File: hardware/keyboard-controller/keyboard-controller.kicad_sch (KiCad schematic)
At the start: 30 parts, among them J1 Keybed_Connector, J2 Debug_Pins, J3 Barrel_Jack_Switch, J4 CV_OUT, J5 GATE_OUT, U1 L78L09_TO92, U2 LM358, U3 74HC164, U4 74HC164, U5 LM1117-3.3, U6 Pico, U7 TL431LP, U8 MCP4921

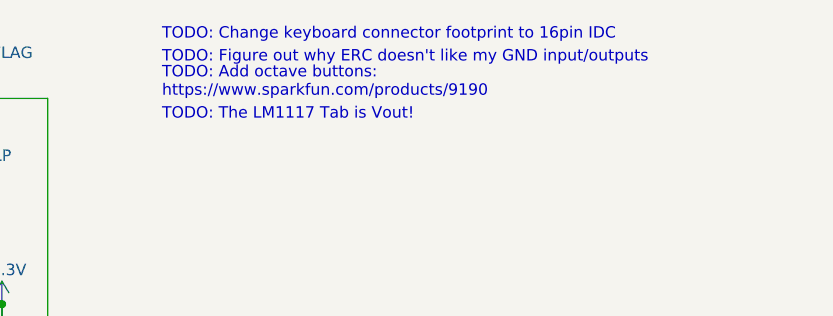
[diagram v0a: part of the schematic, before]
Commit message: Code cleanup. Switched keyboard connector to 16pin IDC
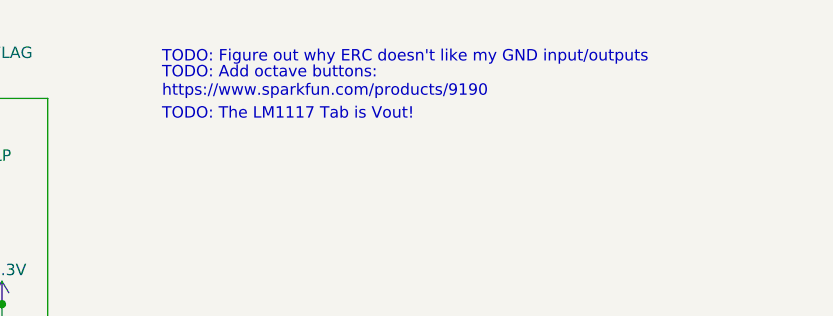
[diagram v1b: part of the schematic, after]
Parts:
- J1: footprint Connector_PinHeader_2.54mm:PinHeader_1x15_P2.54mm_Vertical -> Connector_IDC:IDC-Header_2x08_P2.54mm_Vertical
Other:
- note removed: "TODO: Change keyboard connector footprint to 16pin IDC"
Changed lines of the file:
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@@
     (stroke (width 0) (type default) (color 0 0 0 0))
-  )
-  (text "TODO: Change keyboard connector footprint to 16pin IDC"
-    (at 214.63 15.24 0)
-    (effects (font (size 1.27 1.27)) (justify left bottom))
   )
   (text "TODO: The LM1117 Tab is Vout!" (at 214.63 24.13 0)
@@
     (property "Reference" "J1" (id 0) (at 24.13 59.69 0))
     (property "Value" "Keybed_Connector" (id 1) (at 24.13 57.15 0))
-    (property "Footprint" "Connector_PinHeader_2.54mm:PinHeader_1x15_P2.54mm_Vertical" (id 2) (at 21.59 36.83 0)
+    (property "Footprint" "Connector_IDC:IDC-Header_2x08_P2.54mm_Vertical" (id 2) (at 21.59 36.83 0)
       (effects (font (size 1.27 1.27)) hide)
     )
@@
   (symbol (lib_id "power:+3.3V") (at 128.27 92.71 90) (mirror x) (unit 1)
     (in_bom yes) (on_board yes)
-    (property "Reference" "#PWR?" (id 0) (at 132.08 92.71 0)
+    (property "Reference" "#PWR0102" (id 0) (at 132.08 92.71 0)
       (effects (font (size 1.27 1.27)) hide)
     )
@@
     )
     (path "/31770e7f-32b1-45bb-a492-7d715b566d2b"
-      (reference "#PWR?") (unit 1) (value "+3.3V") (footprint "")
+      (reference "#PWR0102") (unit 1) (value "+3.3V") (footprint "")
     )
     (path "/166f34cf-82f0-4a5a-ad24-51c9547c2601"
@@
     )
     (path "/0ad4f42e-3f7d-4f1a-a0d8-8aff92bbf5d3"
-      (reference "J1") (unit 1) (value "Keybed_Connector") (footprint "Connector_PinHeader_2.54mm:PinHeader_1x15_P2.54mm_Vertical")
+      (reference "J1") (unit 1) (value "Keybed_Connector") (footprint "Connector_IDC:IDC-Header_2x08_P2.54mm_Vertical")
     )
     (path "/cf784822-648c-46a3-a790-edcd7292ca65"

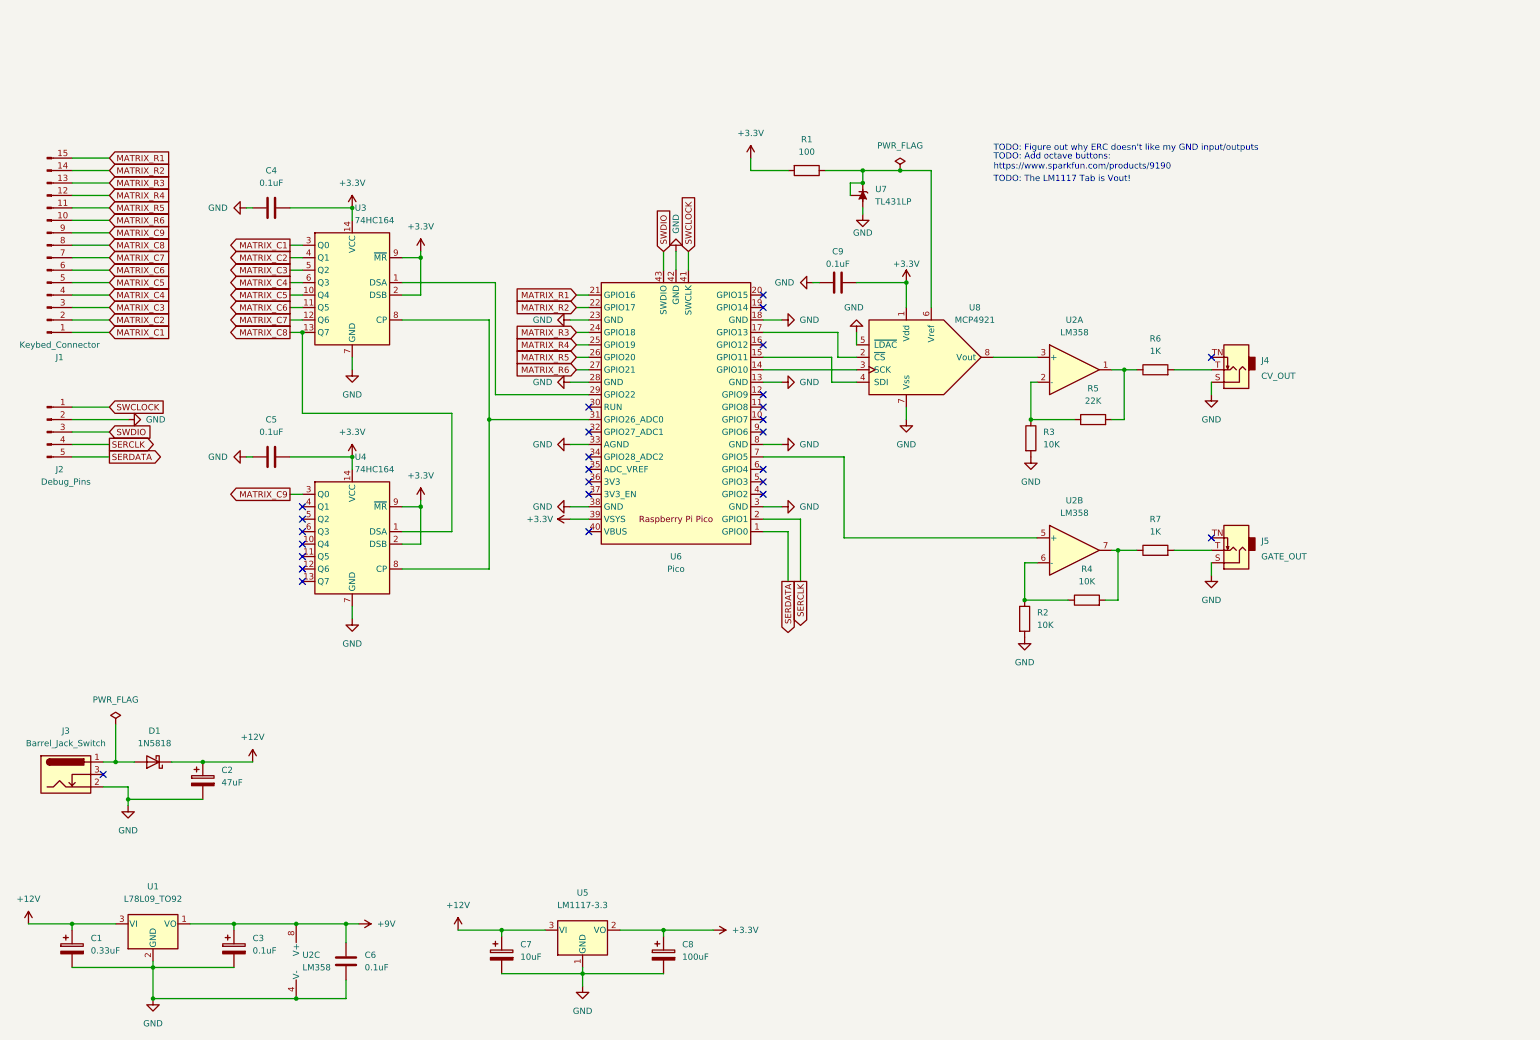
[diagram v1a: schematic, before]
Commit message: Added octave shift buttons
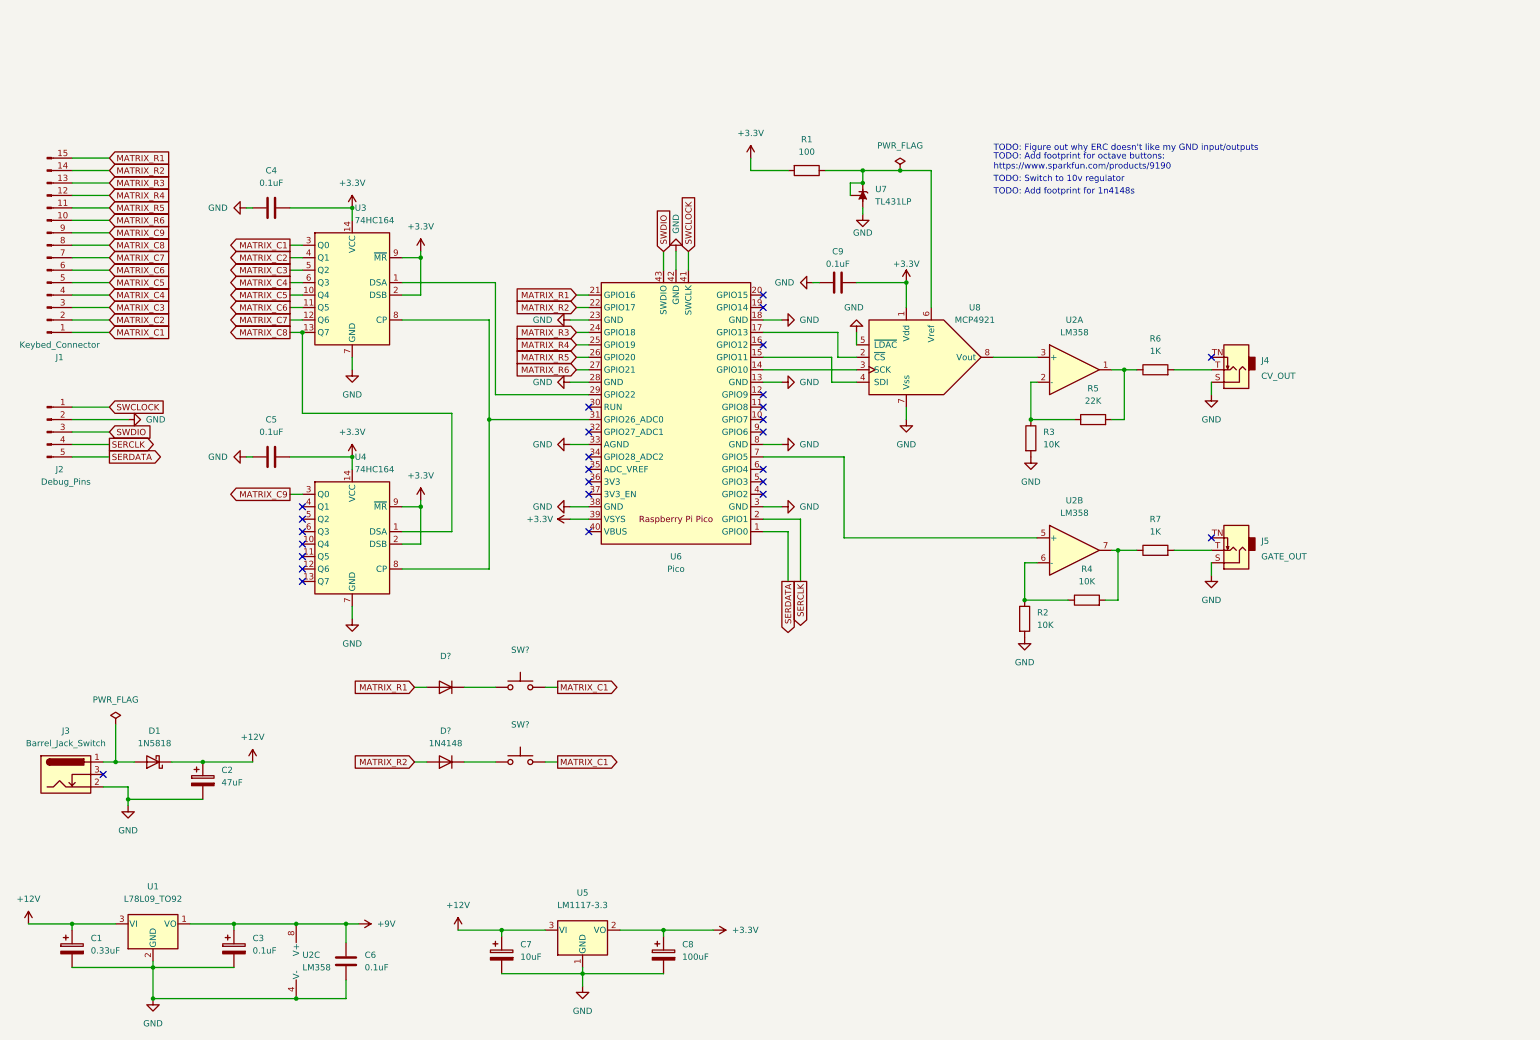
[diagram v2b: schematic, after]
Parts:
- added D?: (no value), symbol Diode:1N4148
- added D?: 1N4148, Diode_THT:D_DO-35_SOD27_P7.62mm_Horizontal, symbol Diode:1N4148
- added SW? (x2): (no value), symbol Switch:SW_Push
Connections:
- net MATRIX_C1: now also SW?.2, SW?.2
- net MATRIX_R1: now also D?.2 (A)
- net MATRIX_R2: now also D?.2 (A)
- new net: D?.1 (K), SW?.1 (x2)
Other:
- note added: "TODO: Add footprint for 1n4148s"
- note added: "TODO: Add footprint for octave buttons: https://www.sparkfun.com/products/9190"
- note added: "TODO: Switch to 10v regulator"
- note removed: "TODO: Add octave buttons: https://www.sparkfun.com/products/9190"
- note removed: "TODO: The LM1117 Tab is Vout!"
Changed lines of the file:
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@@
+    (stroke (width 0) (type default) (color 0 0 0 0))
+  )
+  (wire (pts (xy 106.68 127) (xy 113.03 127))
     (stroke (width 0) (type default) (color 0 0 0 0))
   )
@@
     (stroke (width 0) (type default) (color 0 0 0 0))
   )
+  (wire (pts (xy 96.52 127) (xy 99.06 127))
+    (stroke (width 0) (type default) (color 0 0 0 0))
+  )
   (wire (pts (xy 129.54 59.69) (xy 132.08 59.69))
     (stroke (width 0) (type default) (color 0 0 0 0))
@@
     (stroke (width 0) (type default) (color 0 0 0 0))
   )
+  (wire (pts (xy 96.52 142.24) (xy 99.06 142.24))
+    (stroke (width 0) (type default) (color 0 0 0 0))
+  )
   (wire (pts (xy 165.1 21.59) (xy 172.72 21.59))
     (stroke (width 0) (type default) (color 0 0 0 0))
@@
     (stroke (width 0) (type default) (color 0 0 0 0))
   )
+  (wire (pts (xy 106.68 142.24) (xy 113.03 142.24))
+    (stroke (width 0) (type default) (color 0 0 0 0))
+  )
   (wire (pts (xy 93.98 97.79) (xy 97.79 97.79))
     (stroke (width 0) (type default) (color 0 0 0 0))
@@
     (stroke (width 0) (type default) (color 0 0 0 0))
   )
+  (wire (pts (xy 123.19 127) (xy 125.73 127))
+    (stroke (width 0) (type default) (color 0 0 0 0))
+  )
   (wire (pts (xy 43.18 184.15) (xy 43.18 190.5))
     (stroke (width 0) (type default) (color 0 0 0 0))
@@
     (stroke (width 0) (type default) (color 0 0 0 0))
   )
+  (wire (pts (xy 123.19 142.24) (xy 125.73 142.24))
+    (stroke (width 0) (type default) (color 0 0 0 0))
+  )
   (wire (pts (xy 111.76 102.87) (xy 93.98 102.87))
     (stroke (width 0) (type default) (color 0 0 0 0))
@@
     (stroke (width 0) (type default) (color 0 0 0 0))
   )
-  (text "TODO: The LM1117 Tab is Vout!" (at 214.63 24.13 0)
+  (text "TODO: Switch to 10v regulator" (at 214.63 24.13 0)
+    (effects (font (size 1.27 1.27)) (justify left bottom))
+  )
+  (text "TODO: Add footprint for 1n4148s" (at 214.63 26.67 0)
     (effects (font (size 1.27 1.27)) (justify left bottom))
   )
@@
     (effects (font (size 1.27 1.27)) (justify left bottom))
   )
-  (text "TODO: Add octave buttons:\nhttps://www.sparkfun.com/products/9190"
+  (text "TODO: Add footprint for octave buttons:\nhttps://www.sparkfun.com/products/9190"
     (at 214.63 21.59 0)
     (effects (font (size 1.27 1.27)) (justify left bottom))
@@
     )
   )
+  (global_label "MATRIX_R2" (shape input) (at 96.52 142.24 180) (fields_autoplaced)
+    (effects (font (size 1.27 1.27)) (justify right))
+    (property "Intersheet References" "${INTERSHEET_REFS}" (id 0) (at 84.0679 142.1606 0)
+      (effects (font (size 1.27 1.27)) (justify right) hide)
+    )
+  )
   (global_label "MATRIX_R3" (shape input) (at 34.29 24.13 0) (fields_autoplaced)
     (effects (font (size 1.27 1.27)) (justify left))
@@
     )
   )
+  (global_label "MATRIX_C1" (shape output) (at 125.73 142.24 0) (fields_autoplaced)
+    (effects (font (size 1.27 1.27)) (justify left))
+    (property "Intersheet References" "${INTERSHEET_REFS}" (id 0) (at 138.1821 142.3194 0)
+      (effects (font (size 1.27 1.27)) (justify left) hide)
+    )
+  )
   (global_label "MATRIX_C7" (shape input) (at 34.29 39.37 0) (fields_autoplaced)
     (effects (font (size 1.27 1.27)) (justify left))
@@
     (effects (font (size 1.27 1.27)) (justify left))
     (property "Intersheet References" "${INTERSHEET_REFS}" (id 0) (at 46.7421 46.9106 0)
+      (effects (font (size 1.27 1.27)) (justify left) hide)
+    )
+  )
+  (global_label "MATRIX_R1" (shape input) (at 96.52 127 180) (fields_autoplaced)
+    (effects (font (size 1.27 1.27)) (justify right))
+    (property "Intersheet References" "${INTERSHEET_REFS}" (id 0) (at 84.0679 126.9206 0)
+      (effects (font (size 1.27 1.27)) (justify right) hide)
+    )
+  )
+  (global_label "MATRIX_C1" (shape output) (at 125.73 127 0) (fields_autoplaced)
+    (effects (font (size 1.27 1.27)) (justify left))
+    (property "Intersheet References" "${INTERSHEET_REFS}" (id 0) (at 138.1821 127.0794 0)
       (effects (font (size 1.27 1.27)) (justify left) hide)
     )
@@
     (pin "1")
   )
+  (symbol (lib_id "Diode:1N4148") (at 102.87 127 180) (unit 1)
+    (in_bom yes) (on_board yes) (fields_autoplaced)
+    (property "Reference" "D?" (id 0) (at 102.87 120.65 0))
+    (property "Value" "" (id 1) (at 102.87 123.19 0))
+    (property "Footprint" "" (id 2) (at 102.87 122.555 0)
+      (effects (font (size 1.27 1.27)) hide)
+    )
+    (property "Datasheet" "https://assets.nexperia.com/documents/data-sheet/1N4148_1N4448.pdf" (id 3) (at 102.87 127 0)
+      (effects (font (size 1.27 1.27)) hide)
+    )
+    (pin "1")
+    (pin "2")
+  )
   (symbol (lib_id "Regulator_Linear:L78L09_TO92") (at 43.18 175.26 0) (unit 1)
     (in_bom yes) (on_board yes) (fields_autoplaced)
@@
     (pin "1")
   )
+  (symbol (lib_id "Switch:SW_Push") (at 118.11 127 0) (unit 1)
+    (in_bom yes) (on_board yes) (fields_autoplaced)
+    (property "Reference" "SW?" (id 0) (at 118.11 119.38 0))
+    (property "Value" "" (id 1) (at 118.11 121.92 0))
+    (property "Footprint" "" (id 2) (at 118.11 121.92 0)
+      (effects (font (size 1.27 1.27)) hide)
+    )
+    (property "Datasheet" "~" (id 3) (at 118.11 121.92 0)
+      (effects (font (size 1.27 1.27)) hide)
+    )
+    (pin "1")
+    (pin "2")
+  )
   (symbol (lib_id "power:+3.3V") (at 128.27 92.71 90) (mirror x) (unit 1)
     (in_bom yes) (on_board yes)
@@
     )
     (pin "1")
+  )
+  (symbol (lib_id "Diode:1N4148") (at 102.87 142.24 180) (unit 1)
+    (in_bom yes) (on_board yes) (fields_autoplaced)
+    (property "Reference" "D?" (id 0) (at 102.87 135.89 0))
+    (property "Value" "1N4148" (id 1) (at 102.87 138.43 0))
+    (property "Footprint" "Diode_THT:D_DO-35_SOD27_P7.62mm_Horizontal" (id 2) (at 102.87 137.795 0)
+      (effects (font (size 1.27 1.27)) hide)
+    )
+    (property "Datasheet" "https://assets.nexperia.com/documents/data-sheet/1N4148_1N4448.pdf" (id 3) (at 102.87 142.24 0)
+      (effects (font (size 1.27 1.27)) hide)
+    )
+    (pin "1")
+    (pin "2")
   )
   (symbol (lib_id "Device:R") (at 233.68 109.22 90) (unit 1)
@@
     (pin "9")
   )
+  (symbol (lib_id "Switch:SW_Push") (at 118.11 142.24 0) (unit 1)
+    (in_bom yes) (on_board yes) (fields_autoplaced)
+    (property "Reference" "SW?" (id 0) (at 118.11 134.62 0))
+    (property "Value" "" (id 1) (at 118.11 137.16 0))
+    (property "Footprint" "" (id 2) (at 118.11 137.16 0)
+      (effects (font (size 1.27 1.27)) hide)
+    )
+    (property "Datasheet" "~" (id 3) (at 118.11 137.16 0)
+      (effects (font (size 1.27 1.27)) hide)
+    )
+    (pin "1")
+    (pin "2")
+  )
   (symbol (lib_id "74xx:74HC164") (at 83.82 95.25 0) (mirror y) (unit 1)
     (in_bom yes) (on_board yes) (fields_autoplaced)
@@
       (reference "D1") (unit 1) (value "1N5818") (footprint "Diode_THT:D_DO-41_SOD81_P10.16mm_Horizontal")
     )
+    (path "/1fef29ef-3fc2-4d88-9d07-3199effe6653"
+      (reference "D?") (unit 1) (value "1N4148") (footprint "Diode_THT:D_DO-35_SOD27_P7.62mm_Horizontal")
+    )
+    (path "/3fc229d5-3a51-4ead-9b52-80f5b5c3bb53"
+      (reference "D?") (unit 1) (value "1N4148") (footprint "Diode_THT:D_DO-35_SOD27_P7.62mm_Horizontal")
+    )
     (path "/0ad4f42e-3f7d-4f1a-a0d8-8aff92bbf5d3"
       (reference "J1") (unit 1) (value "Keybed_Connector") (footprint "Connector_IDC:IDC-Header_2x08_P2.54mm_Vertical")
@@
       (reference "R7") (unit 1) (value "1K") (footprint "Royal_Ohm_Resistors:R_Axial_DIN0207_L6.8mm_D2.5mm_P10.16mm_Horizontal")
     )
+    (path "/31550343-14d8-4646-8cd8-824e61793bd2"
+      (reference "SW?") (unit 1) (value "OCTAVE_DOWN") (footprint "")
+    )
+    (path "/4f0145ab-71cf-44d2-86e2-ec66278a135d"
+      (reference "SW?") (unit 1) (value "OCTAVE_UP") (footprint "")
+    )
     (path "/256b7eae-f841-478a-974b-5cf339654f2c"
